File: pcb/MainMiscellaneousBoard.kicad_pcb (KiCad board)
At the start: 2 copper layers, 66 x 60 mm, 24 parts, among them J2 Micro_SD_Card, J3 Micro_SD_Card, U1 ItsyBitsy_ESP32, U2 Seeed_Studio_XIAO-ESP32-S3-Se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

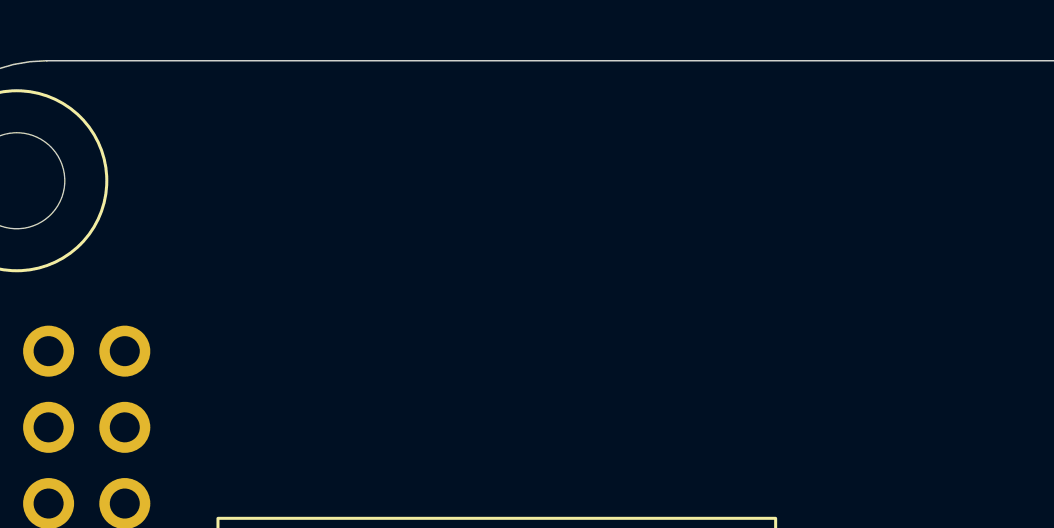
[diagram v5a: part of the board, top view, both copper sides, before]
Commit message: Added in some miscellaneous connectors.
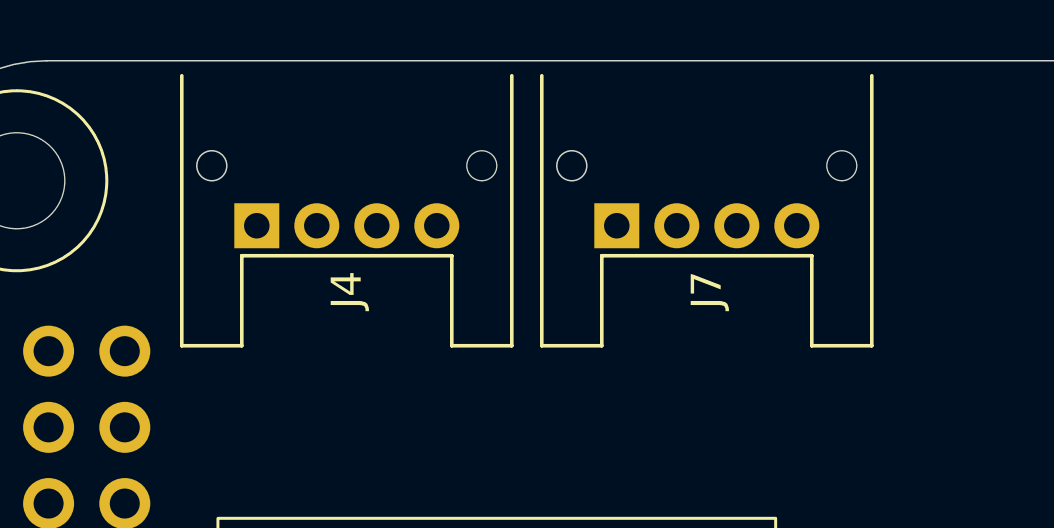
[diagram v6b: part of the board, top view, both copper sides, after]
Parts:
- added J4: S04B-PASK-2, pcb:S04B-PASK-2, F.Cu at (129.0, 75.5)
- added J7: S04B-PASK-2, pcb:S04B-PASK-2, F.Cu at (141.0, 75.5)

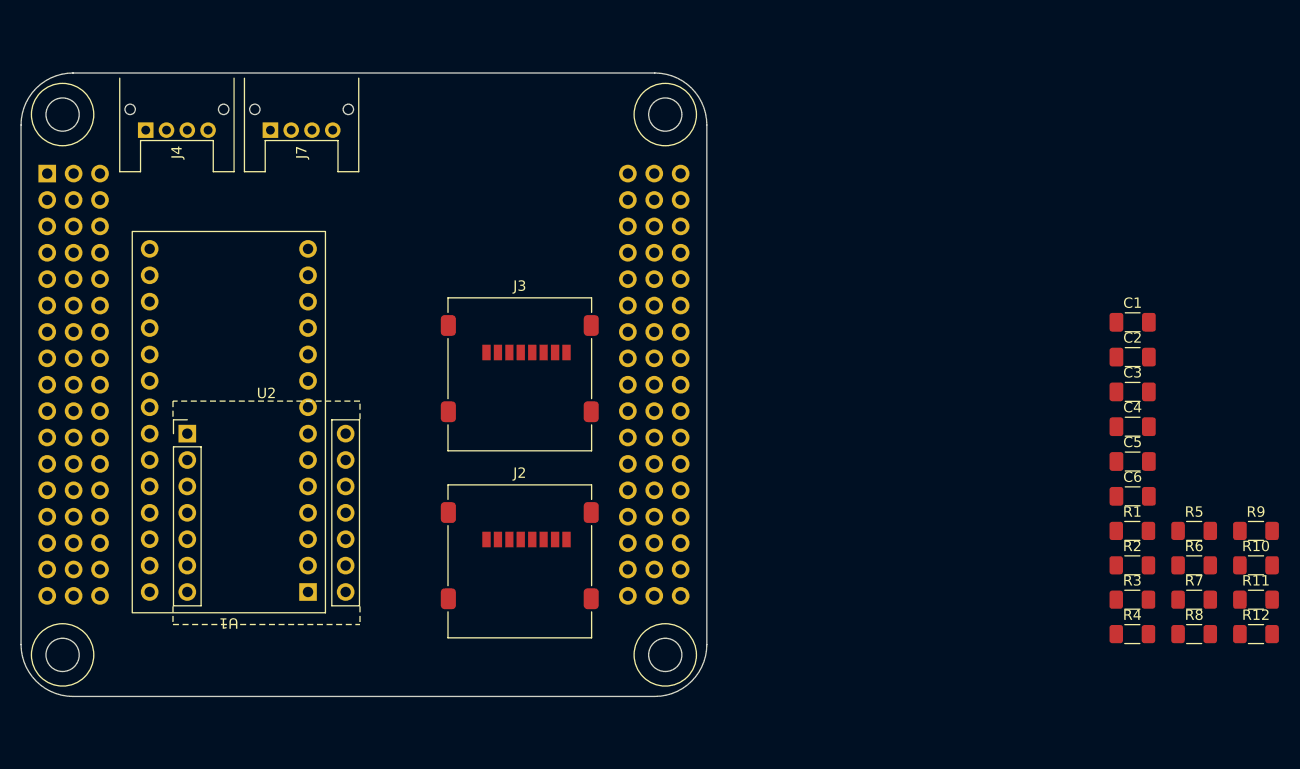
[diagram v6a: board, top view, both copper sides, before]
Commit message: Updated footprints for stack connector's new asymmetry.
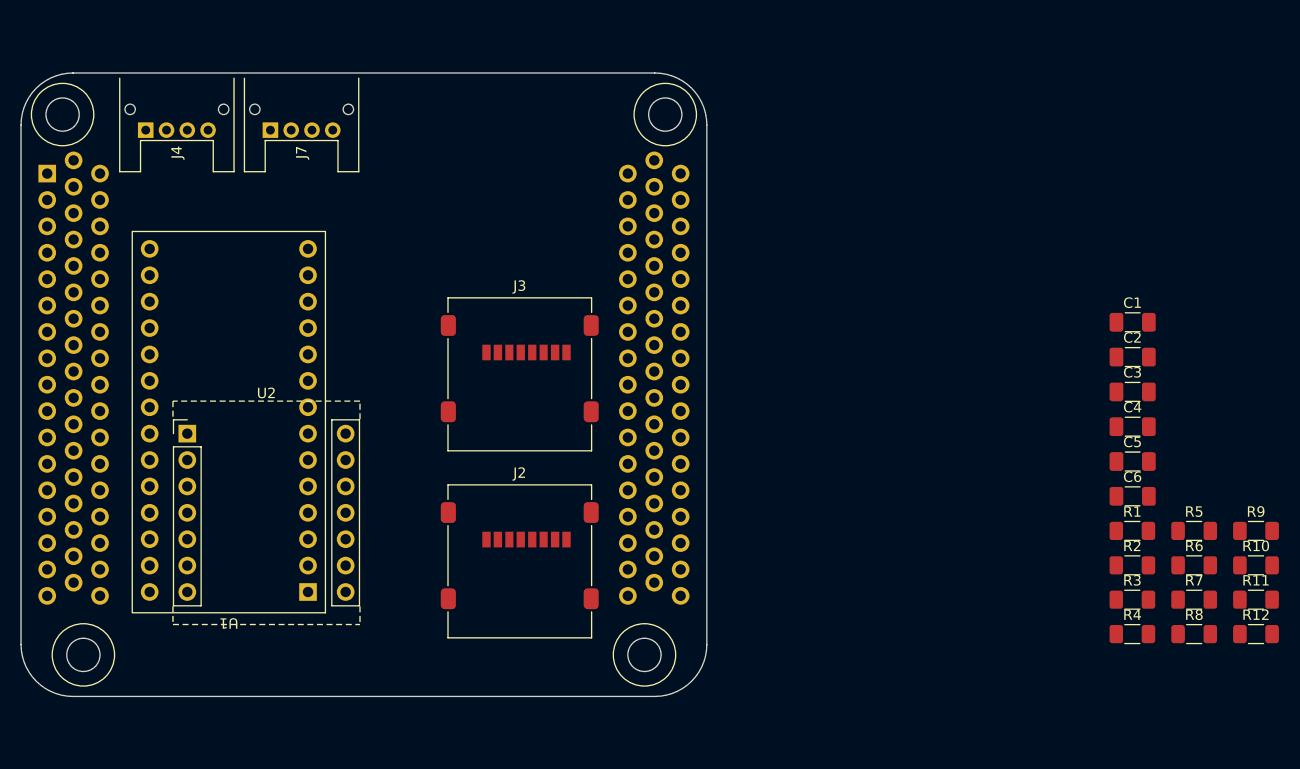
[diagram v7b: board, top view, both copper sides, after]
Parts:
- U1: value ItsyBitsy_ESP32 -> Untitled
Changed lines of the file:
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@@
 		)
 		(fp_circle
-			(center -29 26)
-			(end -26 26)
+			(center -27 26)
+			(end -24 26)
 			(stroke
 				(width 0.1)
@@
 		)
 		(fp_circle
-			(center 29 -26)
-			(end 32 -26)
+			(center 27 26)
+			(end 30 26)
 			(stroke
 				(width 0.1)
@@
 		)
 		(fp_circle
-			(center 29 26)
-			(end 32 26)
+			(center 29 -26)
+			(end 32 -26)
 			(stroke
 				(width 0.1)
@@
 		)
 		(fp_circle
-			(center -29 26)
-			(end -32 26)
+			(center -27 26)
+			(end -30 26)
 			(stroke
 				(width 0.1)
@@
 		)
 		(fp_circle
-			(center 29 -26)
-			(end 26 -26)
+			(center 27 26)
+			(end 24 26)
 			(stroke
 				(width 0.1)
@@
 		)
 		(fp_circle
-			(center 29 26)
-			(end 26 26)
+			(center 29 -26)
+			(end 26 -26)
 			(stroke
 				(width 0.1)
@@
 		)
 		(pad "" np_thru_hole circle
-			(at -29 26)
+			(at -27 26)
 			(size 3.2 3.2)
 			(drill 3.2)
@@
 		)
 		(pad "" np_thru_hole circle
-			(at 29 -26)
+			(at 27 26)
 			(size 3.2 3.2)
 			(drill 3.2)
@@
 		)
 		(pad "" np_thru_hole circle
-			(at 29 26)
+			(at 29 -26)
 			(size 3.2 3.2)
 			(drill 3.2)
@@
 		)
 		(pad "18" thru_hole circle
-			(at -27.94 -20.32)
+			(at -27.94 -21.59)
 			(size 1.7 1.7)
 			(drill 1)
@@
 		)
 		(pad "19" thru_hole circle
-			(at -27.94 -17.78)
+			(at -27.94 -19.05)
 			(size 1.7 1.7)
 			(drill 1)
@@
 		)
 		(pad "20" thru_hole circle
-			(at -27.94 -15.24)
+			(at -27.94 -16.51)
 			(size 1.7 1.7)
 			(drill 1)
@@
 		)
 		(pad "21" thru_hole circle
-			(at -27.94 -12.7)
+			(at -27.94 -13.97)
 			(size 1.7 1.7)
 			(drill 1)
@@
 		)
 		(pad "22" thru_hole oval
-			(at -27.94 -10.16)
+			(at -27.94 -11.43)
 			(size 1.7 1.7)
 			(drill 1)
@@
 		)
 		(pad "23" thru_hole circle
-			(at -27.94 -7.62)
+			(at -27.94 -8.89)
 			(size 1.7 1.7)
 			(drill 1)
@@
 		)
 		(pad "24" thru_hole circle
-			(at -27.94 -5.08)
+			(at -27.94 -6.35)
 			(size 1.7 1.7)
 			(drill 1)
@@
 		)
 		(pad "25" thru_hole circle
-			(at -27.94 -2.54)
+			(at -27.94 -3.81)
 			(size 1.7 1.7)
 			(drill 1)
@@
 		)
 		(pad "26" thru_hole circle
-			(at -27.94 0)
+			(at -27.94 -1.27)
 			(size 1.7 1.7)
 			(drill 1)
@@
 		)
 		(pad "27" thru_hole circle
-			(at -27.94 2.54)
+			(at -27.94 1.27)
 			(size 1.7 1.7)
 			(drill 1)
@@
 		)
 		(pad "28" thru_hole circle
-			(at -27.94 5.08)
+			(at -27.94 3.81)
 			(size 1.7 1.7)
 			(drill 1)
@@
 		)
 		(pad "29" thru_hole circle
-			(at -27.94 7.62)
+			(at -27.94 6.35)
 			(size 1.7 1.7)
 			(drill 1)
@@
 		)
 		(pad "30" thru_hole circle
-			(at -27.94 10.16)
+			(at -27.94 8.89)
 			(size 1.7 1.7)
 			(drill 1)
@@
 		)
 		(pad "31" thru_hole circle
-			(at -27.94 12.7)
+			(at -27.94 11.43)
 			(size 1.7 1.7)
 			(drill 1)
@@
 		)
 		(pad "32" thru_hole circle
-			(at -27.94 15.24)
+			(at -27.94 13.97)
 			(size 1.7 1.7)
 			(drill 1)
@@
 		)
 		(pad "33" thru_hole circle
-			(at -27.94 17.78)
+			(at -27.94 16.51)
 			(size 1.7 1.7)
 			(drill 1)
@@
 		)
 		(pad "34" thru_hole circle
-			(at -27.94 20.32)
+			(at -27.94 19.05)
 			(size 1.7 1.7)
 			(drill 1)
@@
 		)
 		(pad "69" thru_hole circle
-			(at 27.94 -20.32)
+			(at 27.94 -21.59)
 			(size 1.7 1.7)
 			(drill 1)
@@
 		)
 		(pad "70" thru_hole circle
-			(at 27.94 -17.78)
+			(at 27.94 -19.05)
 			(size 1.7 1.7)
 			(drill 1)
@@
 		)
 		(pad "71" thru_hole circle
-			(at 27.94 -15.24)
+			(at 27.94 -16.51)
 			(size 1.7 1.7)
 			(drill 1)
@@
 		)
 		(pad "72" thru_hole circle
-			(at 27.94 -12.7)
+			(at 27.94 -13.97)
 			(size 1.7 1.7)
 			(drill 1)
@@
 		)
 		(pad "73" thru_hole circle
-			(at 27.94 -10.16)
+			(at 27.94 -11.43)
 			(size 1.7 1.7)
 			(drill 1)
@@
 		)
 		(pad "74" thru_hole circle
-			(at 27.94 -7.62)
+			(at 27.94 -8.89)
 			(size 1.7 1.7)
 			(drill 1)
@@
 		)
 		(pad "75" thru_hole circle
-			(at 27.94 -5.08)
+			(at 27.94 -6.35)
 			(size 1.7 1.7)
 			(drill 1)
@@
 		)
 		(pad "76" thru_hole circle
-			(at 27.94 -2.54)
+			(at 27.94 -3.81)
 			(size 1.7 1.7)
 			(drill 1)
@@
 		)
 		(pad "77" thru_hole circle
-			(at 27.94 0)
+			(at 27.94 -1.27)
 			(size 1.7 1.7)
 			(drill 1)
@@
 		)
 		(pad "78" thru_hole circle
-			(at 27.94 2.54)
+			(at 27.94 1.27)
 			(size 1.7 1.7)
 			(drill 1)
@@
 		)
 		(pad "79" thru_hole circle
-			(at 27.94 5.08)
+			(at 27.94 3.81)
 			(size 1.7 1.7)
 			(drill 1)
@@
 		)
 		(pad "80" thru_hole circle
-			(at 27.94 7.62)
+			(at 27.94 6.35)
 			(size 1.7 1.7)
 			(drill 1)
@@
 		)
 		(pad "81" thru_hole circle
-			(at 27.94 10.16)
+			(at 27.94 8.89)
 			(size 1.7 1.7)
 			(drill 1)
@@
 		)
 		(pad "82" thru_hole circle
-			(at 27.94 12.7)
+			(at 27.94 11.43)
 			(size 1.7 1.7)
 			(drill 1)
@@
 		)
 		(pad "83" thru_hole circle
-			(at 27.94 15.24)
+			(at 27.94 13.97)
 			(size 1.7 1.7)
 			(drill 1)
@@
 		)
 		(pad "84" thru_hole circle
-			(at 27.94 17.78)
+			(at 27.94 16.51)
 			(size 1.7 1.7)
 			(drill 1)
@@
 		)
 		(pad "85" thru_hole circle
-			(at 27.94 20.32)
+			(at 27.94 19.05)
 			(size 1.7 1.7)
 			(drill 1)
@@
 		(model "${KIPRJMOD}/models/StackingHeader_2.54mm_1x17.step"
 			(offset
-				(xyz -27.95 20.3 0)
+				(xyz -27.95000001 21.56999999 0)
 			)
 			(scale
@@
 		(model "${KIPRJMOD}/models/StackingHeader_2.54mm_1x17.step"
 			(offset
-				(xyz 27.95 20.3 0)
+				(xyz 27.95000001 21.56999999 0)
 			)
 			(scale
@@
 		(fp_line
 			(start -4 -2.5)
-			(end -4.000001 -0.5)
+			(end -4 -0.5)
 			(stroke
 				(width 0.12)
@@
 		)
 		(fp_line
-			(start -4.000001 -0.5)
+			(start -4 -0.5)
 			(end -1 -0.5)
 			(stroke
@@
 		(fp_line
 			(start -4 6.5)
-			(end -4 8.500001)
+			(end -4 8.5)
 			(stroke
 				(width 0.12)
@@
 		)
 		(fp_line
-			(start -4 8.500001)
-			(end 5 8.500001)
+			(start -4 8.5)
+			(end 5 8.5)
 			(stroke
 				(width 0.12)
@@
 		)
 		(fp_circle
-			(center 2 7.499999)
+			(center 2 7.5)
 			(end 2.5 7.5)
 			(stroke
@@
 		)
 		(pad "2" thru_hole circle
-			(at 0 2.000001)
+			(at 0 2)
 			(size 1.5 1.5)
 			(drill 0.85)
@@
 			)
 		)
-		(property "Value" "ItsyBitsy_ESP32"
+		(property "Value" "Untitled"
 			(at 0 1 180)
 			(unlocked yes)
@@
 		(clearance 0)
 		(attr through_hole)
-		(fp_poly
-			(pts
-				(xy -1.674999 -2) (xy 16.915 -2) (xy 16.915 34.695) (xy -1.675 34.695)
-			)
+		(fp_rect
+			(start -1.675 -2)
+			(end 16.915 34.695)
 			(stroke
 				(width 0.1)
@@
 		)
 		(pad "3" thru_hole circle
-			(at 0 5.079999 180)
+			(at 0 5.08 180)
 			(size 1.7 1.7)
 			(drill 1)
@@
 		)
 		(pad "8" thru_hole circle
-			(at 0 17.780001 180)
+			(at 0 17.78 180)
 			(size 1.7 1.7)
 			(drill 1)
@@
 		)
 		(pad "12" thru_hole circle
-			(at 0 27.939999 180)
+			(at 0 27.94 180)
 			(size 1.7 1.7)
 			(drill 1)
@@
 		(fp_line
 			(start -4 -2.5)
-			(end -4.000001 -0.5)
+			(end -4 -0.5)
 			(stroke
 				(width 0.12)
@@
 		)
 		(fp_line
-			(start -4.000001 -0.5)
+			(start -4 -0.5)
 			(end -1 -0.5)
 			(stroke
@@
 		(fp_line
 			(start -4 6.5)
-			(end -4 8.500001)
+			(end -4 8.5)
 			(stroke
 				(width 0.12)
@@
 		)
 		(fp_line
-			(start -4 8.500001)
-			(end 5 8.500001)
+			(start -4 8.5)
+			(end 5 8.5)
 			(stroke
 				(width 0.12)
@@
 		)
 		(fp_circle
-			(center 2 7.499999)
+			(center 2 7.5)
 			(end 2.5 7.5)
 			(stroke
@@
 		)
 		(pad "2" thru_hole circle
-			(at 0 2.000001)
+			(at 0 2)
 			(size 1.5 1.5)
 			(drill 0.85)

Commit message: Virtual housing model for `MainMiscellaneousBoard`.
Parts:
- N1: footprint pcb:MainMiscellaneousBoardHousing -> pcb:Dummy
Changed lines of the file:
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@@
 		)
 	)
-	(footprint "pcb:MainMiscellaneousBoardHousing"
+	(footprint "pcb:Dummy"
 		(locked yes)
 		(layer "F.Cu")
 		(at 150 100)
-		(descr "Housing for the Main Camera System.")
 		(property "Reference" "N1"
 			(at 0 -0.5 0)
@@
 			)
 		)
-		(property "Datasheet" "~"
+		(property "Datasheet" ""
 			(at 0 0 0)
 			(unlocked yes)
@@
 			)
 		)
-		(property "Description" "Housing"
+		(property "Description" ""
 			(at 0 0 0)
 			(unlocked yes)
@@
 			)
 		)
-		(property ki_fp_filters "Enclosure* Housing*")
-		(sheetname "/")
-		(sheetfile "MainMiscellaneousBoard.kicad_sch")
+		(attr exclude_from_bom)
 		(fp_line
 			(start -1 0)
@@
 		)
 		(embedded_fonts no)
+		(model "${KIPRJMOD}/models/ElectronicsBoxCase_AN-14F-01_Body.step"
+			(opacity 0.3600)
+			(offset
+				(xyz 0 17.5 -2)
+			)
+			(scale
+				(xyz 1 1 1)
+			)
+			(rotate
+				(xyz -90 -0 -0)
+			)
+		)
+		(model "${KIPRJMOD}/models/amphenol_female_66_pins_TVS07RK19-35P.stp"
+			(offset
+				(xyz 0 44.5 -64.2)
+			)
+			(scale
+				(xyz 1 1 1)
+			)
+			(rotate
+				(xyz -0 180 -0)
+			)
+		)
+		(model "${KIPRJMOD}/models/Main_Stack_Dummy.step"
+			(opacity 0.5400)
+			(offset
+				(xyz 0 0 -35.1)
+			)
+			(scale
+				(xyz 1 1 1)
+			)
+			(rotate
+				(xyz -0 -0 -0)
+			)
+		)
+		(model "${KIPRJMOD}/models/Main_Stack_Dummy.step"
+			(offset
+				(xyz 0 0 -12.5)
+			)
+			(scale
+				(xyz 1 1 1)
+			)
+			(rotate
+				(xyz -0 -0 -0)
+			)
+		)
+		(model "${KIPRJMOD}/models/ElectronicsBoxCase_AN-14F-01_Lid.step"
+			(opacity 0.5600)
+			(offset
+				(xyz 0 17.5 -2)
+			)
+			(scale
+				(xyz 1 1 1)
+			)
+			(rotate
+				(xyz -90 -0 -0)
+			)
+		)
+		(model "${KIPRJMOD}/models/Main_Stack_Dummy.step"
+			(offset
+				(xyz 0 0 -23.6)
+			)
+			(scale
+				(xyz 1 1 1)
+			)
+			(rotate
+				(xyz -0 -0 -0)
+			)
+		)
 	)
 	(footprint "Resistor_SMD:R_1206_3216Metric_Pad1.30x1.75mm_HandSolder"
